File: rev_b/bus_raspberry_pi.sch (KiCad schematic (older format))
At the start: 47 parts, among them J1 TERMINATE_JUMPER, J2 LED_JUMPER, SW1 MJTP1243, U1 MCP7940, U2 74HCT08, U3 MCP2562, U4 L78L05AC, U5 ATMEGA324_DIP40, U6 L78L33AC, X1 16MHz, X2 32.768KHz

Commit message: Revision B is ready for manufacture.
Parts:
- removed N10: BBB_P9_HEADER, bus_beaglebone:Pin_Header_Straight_2x23, symbol BBB_P9_HEADER
- removed N11, N12, N13: KEY2, bus_beaglebone:Pin_Header_Straight_1x02, symbol KEY2
- removed R6, R7: 4K7, bus_beaglebone:Resistor_Horizontal__400, symbol R_VERT
- added C12, C13: .1uF, bus_raspberry_pi:Capacitor3MMDiscRM2.5, symbol C_VERT
- added N1: RASPI_CONNECTOR_40, bus_raspberry_pi:Pin_Header_Straight_2x20, symbol RASPI_CONNECTOR_40
- added R6: 3K9_SIP5, bus_raspberry_pi:Pin_Header_Straight_1x05, symbol R_VERT_SIP5
- added U7: MCP24XX32A, bus_raspberry_pi:DIP-8__300, symbol MCP24XX32A
- BAT1: footprint bus_beaglebone:10MM_BATTERY -> bus_raspberry_pi:10MM_BATTERY
- C1, C10, C11, C2, C3, C4, C5, C6, C7, C8, C9: footprint bus_beaglebone:Capacitor3MMDiscRM2.5 -> bus_raspberry_pi:Capacitor3MMDiscRM2.5
- D1: footprint bus_beaglebone:Diode_DO-41_SOD81_Horizontal_RM10 -> bus_raspberry_pi:Diode_DO-41_SOD81_Horizontal_RM10
- D2: footprint bus_beaglebone:T1_LED -> bus_raspberry_pi:T1_LED
- H1, H2, H3, H4: footprint bus_beaglebone:MountingHole_3mm -> bus_raspberry_pi:MountingHole_3mm
- H5: footprint bus_beaglebone:OSHW_LOGO_250mil -> bus_raspberry_pi:OSHW_LOGO_250mil
- J1: footprint bus_beaglebone:Pin_Header_Straight_1x03 -> bus_raspberry_pi:Pin_Header_Straight_1x03
- J2: footprint bus_beaglebone:Pin_Header_Straight_2x02 -> bus_raspberry_pi:Pin_Header_Straight_2x02
- N3, N9: footprint bus_beaglebone:Pin_Header_Straight_2x05_Shrouded -> bus_raspberry_pi:Pin_Header_Straight_2x05_Shrouded
- N4, N5, R2: footprint bus_beaglebone:Pin_Header_Straight_1x06 -> bus_raspberry_pi:Pin_Header_Straight_1x06
- N7: footprint bus_beaglebone:Pin_Header_Straight_2x03 -> bus_raspberry_pi:Pin_Header_Straight_2x03
- N8: footprint bus_beaglebone:Pin_Header_Straight_1x04 -> bus_raspberry_pi:Pin_Header_Straight_1x04
- R1, R3, R4, R5: footprint bus_beaglebone:Resistor_Horizontal__400 -> bus_raspberry_pi:Resistor_Horizontal__400
- SW1: footprint bus_beaglebone:Button_6.5MM -> bus_raspberry_pi:Button_6.5MM
- U1, U3: footprint bus_beaglebone:DIP-8__300 -> bus_raspberry_pi:DIP-8__300
- U2: footprint bus_beaglebone:DIP-14__300 -> bus_raspberry_pi:DIP-14__300
- U4, U6: footprint bus_beaglebone:TO92_123 -> bus_raspberry_pi:TO92_123
- U5: footprint bus_beaglebone:DIP-40__600 -> bus_raspberry_pi:DIP-40__600
- X1: footprint bus_beaglebone:Crystal_HC49-U_Vertical -> bus_raspberry_pi:Crystal_HC49-U_Vertical
- X2: footprint bus_beaglebone:RTC_CRYSTAL -> bus_raspberry_pi:RTC_CRYSTAL
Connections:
- net +3.3V: now also C12.1, C13.1, R6.1, R6.1, R6.1, R6.1, U7.8 (VCC)
- net GND: now also C12.2, C13.2, N1.14 (GND), N1.20 (GND), N1.25 (GND), N1.30 (GND), N1.34 (GND), N1.39 (GND), N1.6 (GND), N1.9 (GND), U7.1 (A0), U7.2 (A1), U7.3 (A2), U7.4 (VSS), U7.7 (WP); no longer H1.1 (GND), H2.1 (GND), H3.1 (GND), H4.1 (GND)
- net at U1.6 (SCL), U5.22 (PC0/SCL): now also R6.3
- net at U1.5 (SDA), U5.23 (PC1/SDA): now also R6.2
- net at N5.5 (RXD), N8.2 (TXD), R2.4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: now also N1.8 (GPIO14_TXD0)
- net at N8.3 (RXD), U2.11: now also N1.10 (GPIO15_RXD0)
- net at N8.4 (~RESET), R2.6, U2.9: now also N1.24 (GPIO8_CE0_N)
- new net: N1.27 (EEPROM_ID_SDA), R6.4, U7.5 (SDA)
- new net: N1.28 (EEPROM_I2C_SCL), R6.5, U7.6 (SCL)
- no-connect marks 68 -> 64
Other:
- moved on the sheet: N7, R2E, U2C

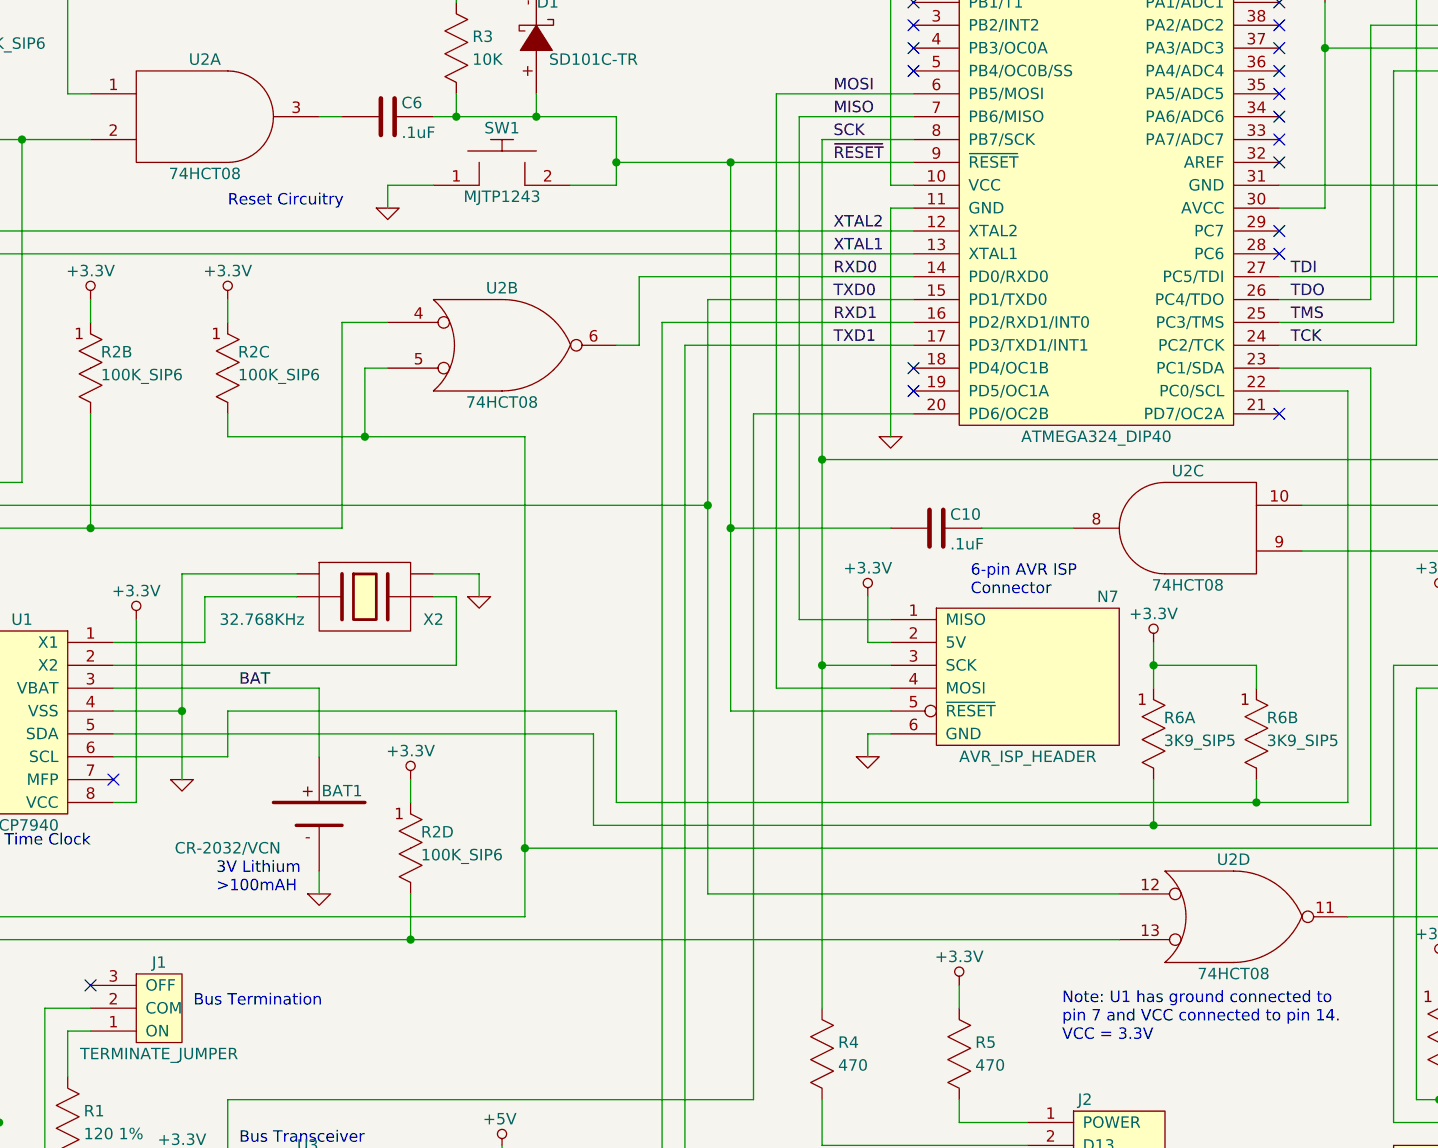
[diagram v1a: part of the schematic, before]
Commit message: Converted 74HCT08 => 74HC08 .
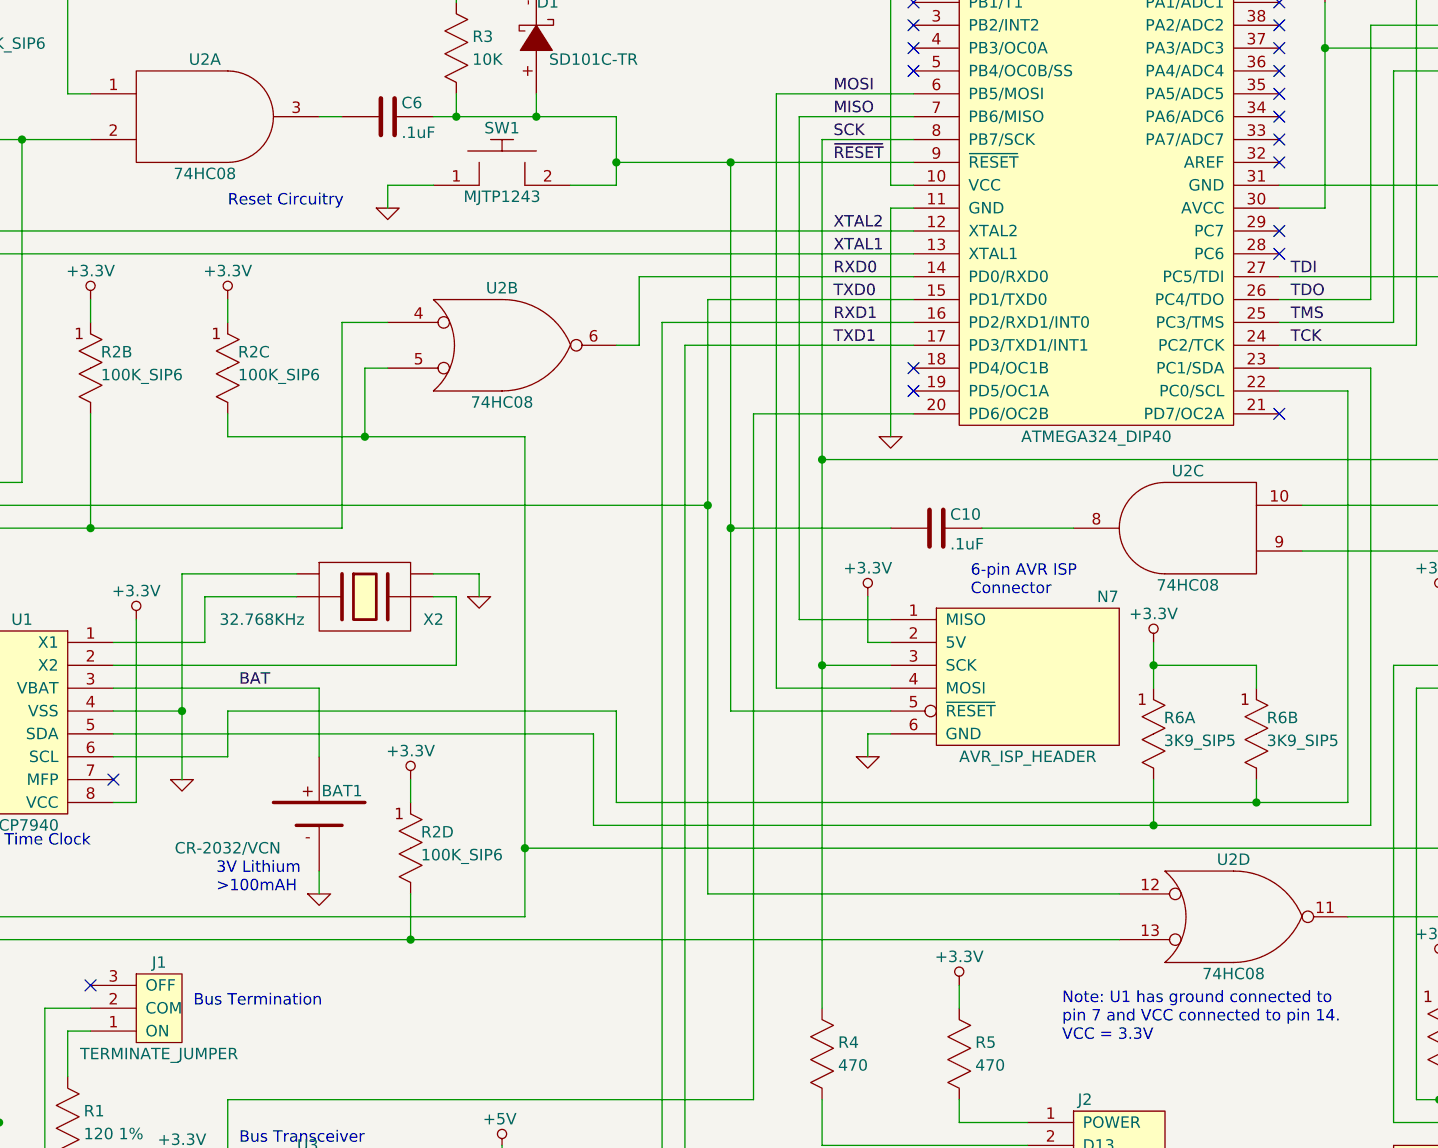
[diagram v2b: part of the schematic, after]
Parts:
- U2: value 74HCT08 -> 74HC08
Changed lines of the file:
@@
 P 3800 2500
 F 0 "U2" H 3800 2750 50  0000 C CNN
-F 1 "74HCT08" H 3800 2250 50  0000 C CNN
+F 1 "74HC08" H 3800 2250 50  0000 C CNN
 F 2 "bus_raspberry_pi:DIP-14__300" H 3800 2500 60  0001 C CNN
 F 3 "" H 3800 2500 60  0000 C CNN
@@
 P 7000 5000
 F 0 "U2" H 7000 5250 50  0000 C CNN
-F 1 "74HCT08" H 7000 4750 50  0000 C CNN
+F 1 "74HC08" H 7000 4750 50  0000 C CNN
 F 2 "bus_raspberry_pi:DIP-14__300" H 7000 5000 60  0001 C CNN
 F 3 "" H 7000 5000 60  0000 C CNN
@@
 P 2500 1500
 F 0 "U2" H 2500 1750 50  0000 C CNN
-F 1 "74HCT08" H 2500 1250 50  0000 C CNN
+F 1 "74HC08" H 2500 1250 50  0000 C CNN
 F 2 "bus_raspberry_pi:DIP-14__300" H 2500 1500 60  0001 C CNN
 F 3 "" H 2500 1500 60  0000 C CNN
@@
 P 6800 3300
 F 0 "U2" H 6800 3050 50  0000 C CNN
-F 1 "74HCT08" H 6800 3550 50  0000 C CNN
+F 1 "74HC08" H 6800 3550 50  0000 C CNN
 F 2 "bus_raspberry_pi:DIP-14__300" H 6800 3300 60  0001 C CNN
 F 3 "" H 6800 3300 60  0000 C CNN
